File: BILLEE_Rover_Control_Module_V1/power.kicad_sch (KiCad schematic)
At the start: 86 parts, among them CN1 XT90PW-M.G.Y, CN2 XT60PW-M, CN3 XT60PW-M, CN4 XT60PW-M, CN5 XT60PW-M, SW1 33uH, U1 INA780BIDEKR, U2 MCP9808T-E/MS, U3 TPS1HA08BQPWPRQ1, U4 TPS1HA08BQPWPRQ1, U5 TPS1HA08BQPWPRQ1, U6 LT8612EUDE#TRPBF, U7 LT8612EUDE#TRPBF, U8 LT8612EUDE#TRPBF, U9 10uH

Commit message: continuing layout
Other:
- note added: "(+22.2v -> +12V) Network Switch and Aux Power"
- note removed: "+12V Network Switch and Aux Power"
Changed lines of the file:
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@@
 		)
 	)
-	(text "+12V Network Switch and Aux Power"
+	(text "(+22.2v -> +12V) Network Switch and Aux Power"
 		(exclude_from_sim no)
 		(at 96.012 171.958 0)
@@
 		)
 	)
-	(netclass_flag ""
-		(length 2.54)
-		(shape round)
-		(at 328.93 96.52 0)
-		(fields_autoplaced yes)
-		(effects
-			(font
-				(size 1.27 1.27)
-			)
-			(justify left bottom)
-		)
-		(property "Net Class" ""
-			(at 101.6 125.73 0)
-			(show_name no)
-			(do_not_autoplace no)
-			(effects
-				(font
-					(size 1.27 1.27)
-				)
-			)
-		)
-		(property "Component Class" "Jetsonregs"
-			(at 329.6285 93.98 0)
-			(show_name no)
-			(do_not_autoplace no)
-			(effects
-				(font
-					(size 1.27 1.27)
-					(italic yes)
-				)
-				(justify left)
-			)
-		)
-	)
 	(symbol
 		(lib_id "power:GND")
@@
 		(in_pos_files yes)
 		(dnp no)
-		(fields_autoplaced yes)
 		(property "Reference" "#PWR043"
 			(at 262.89 165.1 0)
@@
 		)
 		(property "Value" "GND"
-			(at 262.89 163.83 0)
+			(at 267.716 160.274 0)
 			(show_name no)
 			(do_not_autoplace no)

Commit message: Layout Cont.
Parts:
- removed TP2: TestPoint, TestPoint:TestPoint_THTPad_2.0x2.0mm_Drill1.0mm, symbol Connector:TestPoint
- added H1, H2, H3, H4: MountingHole_Pad, MountingHole:MountingHole_5.3mm_M5_Pad_Via, symbol Mechanical:MountingHole_Pad
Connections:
- net GND: now also CN4.3, CN4.4
- new net CHA_GND: H1.1, H2.1, H3.1, H4.1

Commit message: Layout! 🍋
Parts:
- H1, H2, H3, H4: footprint MountingHole:MountingHole_5.3mm_M5_Pad_Via -> MountingHole:MountingHole_4.3mm_M4_Pad_Via
- R22, R24, R26: value 180k -> 200k

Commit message: Layout!
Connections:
- net CHA_GND is gone; now on net GND: H1.1, H2.1, H3.1, H4.1
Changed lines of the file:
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@@
 	)
 	(junction
-		(at 52.07 184.15)
-		(diameter 0)
-		(color 0 0 0 0)
-	)
-	(junction
 		(at 59.69 133.35)
 		(diameter 0)
@@
 	)
 	(junction
+		(at 52.07 184.15)
+		(diameter 0)
+		(color 0 0 0 0)
+	)
+	(junction
 		(at 209.55 46.99)
 		(diameter 0)
@@
 	(wire
 		(pts
-			(xy 52.07 184.15) (xy 68.58 184.15)
-		)
-		(stroke
-			(width 0)
-			(type default)
-		)
-	)
-	(wire
-		(pts
 			(xy 134.62 187.96) (xy 171.45 187.96)
 		)
@@
 	(wire
 		(pts
+			(xy 52.07 184.15) (xy 68.58 184.15)
+		)
+		(stroke
+			(width 0)
+			(type default)
+		)
+	)
+	(wire
+		(pts
 			(xy 220.98 189.23) (xy 241.3 189.23)
 		)
@@
 	)
 	(symbol
-		(lib_id "power:GNDPWR")
-		(at 52.07 184.15 0)
-		(unit 1)
-		(body_style 1)
-		(exclude_from_sim no)
-		(in_bom yes)
-		(on_board yes)
-		(in_pos_files yes)
-		(dnp no)
-		(fields_autoplaced yes)
-		(property "Reference" "#PWR0209"
-			(at 52.07 189.23 0)
-			(hide yes)
-			(show_name no)
-			(do_not_autoplace no)
-			(effects
-				(font
-					(size 1.27 1.27)
-				)
-			)
-		)
-		(property "Value" "CHA_GND"
-			(at 51.943 187.96 0)
-			(show_name no)
-			(do_not_autoplace no)
-			(effects
-				(font
-					(size 1.27 1.27)
-				)
-			)
-		)
-		(property "Footprint" ""
-			(at 52.07 185.42 0)
-			(hide yes)
-			(show_name no)
-			(do_not_autoplace no)
-			(effects
-				(font
-					(size 1.27 1.27)
-				)
-			)
-		)
-		(property "Datasheet" ""
-			(at 52.07 185.42 0)
-			(hide yes)
-			(show_name no)
-			(do_not_autoplace no)
-			(effects
-				(font
-					(size 1.27 1.27)
-				)
-			)
-		)
-		(property "Description" "Power symbol creates a global label with name \"GNDPWR\" , global ground"
-			(at 52.07 184.15 0)
-			(hide yes)
-			(show_name no)
-			(do_not_autoplace no)
-			(effects
-				(font
-					(size 1.27 1.27)
-				)
-			)
-		)
-		(pin "1"
-		)
-		(instances
-			(project "BILLEE_Rover_Control_Module_V1"
-				(path "/e701dc98-f022-461d-84b5-6b2dd8d89d58/e37b5ac2-398e-41bf-8fb6-2ff87cb1df37"
-					(reference "#PWR0209")
-					(unit 1)
-				)
-			)
-		)
-	)
-	(symbol
 		(lib_id "power:GND")
 		(at 237.49 149.86 0)
@@
 					(unit 1)
 				)
+			)
+		)
+	)
+	(symbol
+		(lib_id "power:GND")
+		(at 52.07 184.15 0)
+		(unit 1)
+		(body_style 1)
+		(exclude_from_sim no)
+		(in_bom yes)
+		(on_board yes)
+		(in_pos_files yes)
+		(dnp no)
+		(fields_autoplaced yes)
+		(property "Reference" "#PWR0209"
+			(at 52.07 190.5 0)
+			(hide yes)
+			(show_name no)
+			(do_not_autoplace no)
+			(effects
+				(font
+					(size 1.27 1.27)
+				)
+			)
+		)
+		(property "Value" "GND"
+			(at 52.07 189.23 0)
+			(show_name no)
+			(do_not_autoplace no)
+			(effects
+				(font
+					(size 1.27 1.27)
+				)
+			)
+		)
+		(property "Footprint" ""
+			(at 52.07 184.15 0)
+			(hide yes)
+			(show_name no)
+			(do_not_autoplace no)
+			(effects
+				(font
+					(size 1.27 1.27)
+				)
+			)
+		)
+		(property "Datasheet" ""
+			(at 52.07 184.15 0)
+			(hide yes)
+			(show_name no)
+			(do_not_autoplace no)
+			(effects
+				(font
+					(size 1.27 1.27)
+				)
+			)
+		)
+		(property "Description" "Power symbol creates a global label with name \"GND\" , ground"
+			(at 52.07 184.15 0)
+			(hide yes)
+			(show_name no)
+			(do_not_autoplace no)
+			(effects
+				(font
+					(size 1.27 1.27)
+				)
+			)
+		)
+		(pin "1"
+		)
+		(instances
+			(project "BILLEE_Rover_Control_Module_V1"
+				(path "/e701dc98-f022-461d-84b5-6b2dd8d89d58/e37b5ac2-398e-41bf-8fb6-2ff87cb1df37"
+					(reference "#PWR0209")
+					(unit 1)
+				)

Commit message: More layout :tired_face:
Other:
- moved on the sheet: C12, C15, C18, C21, C24, C3, C6, C72, C9, CN4, CN5, D3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

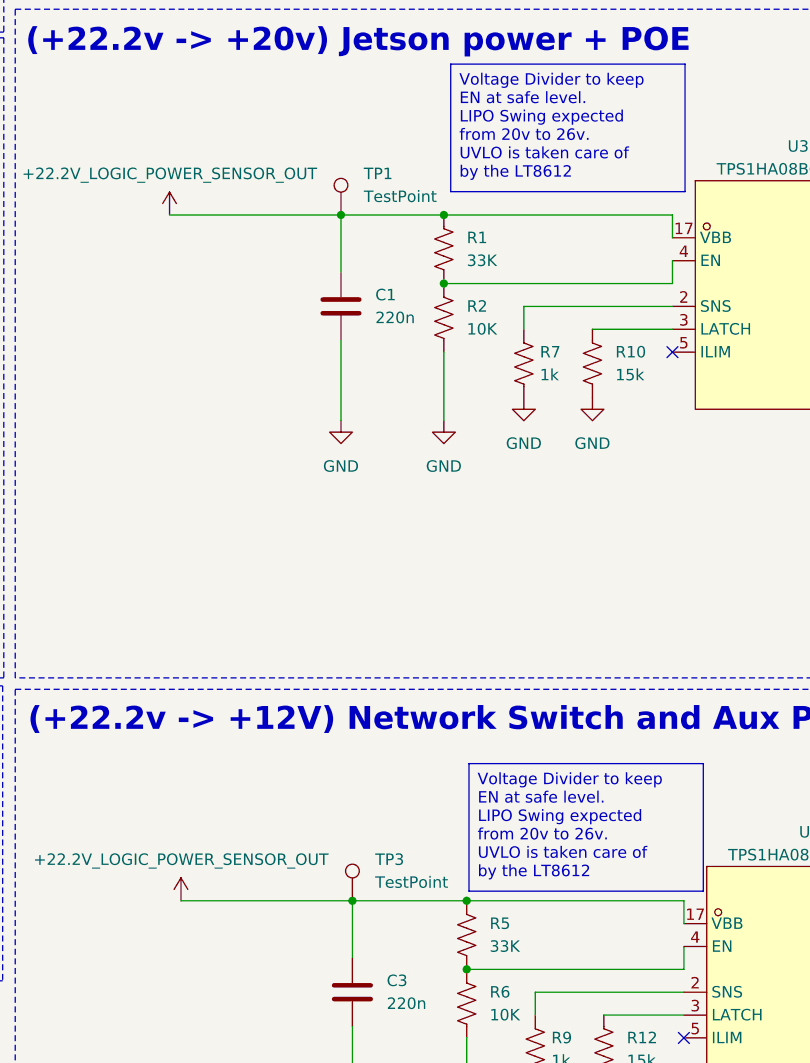
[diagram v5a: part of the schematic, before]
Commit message: Resatarted Layout for something a little bit cleaner.
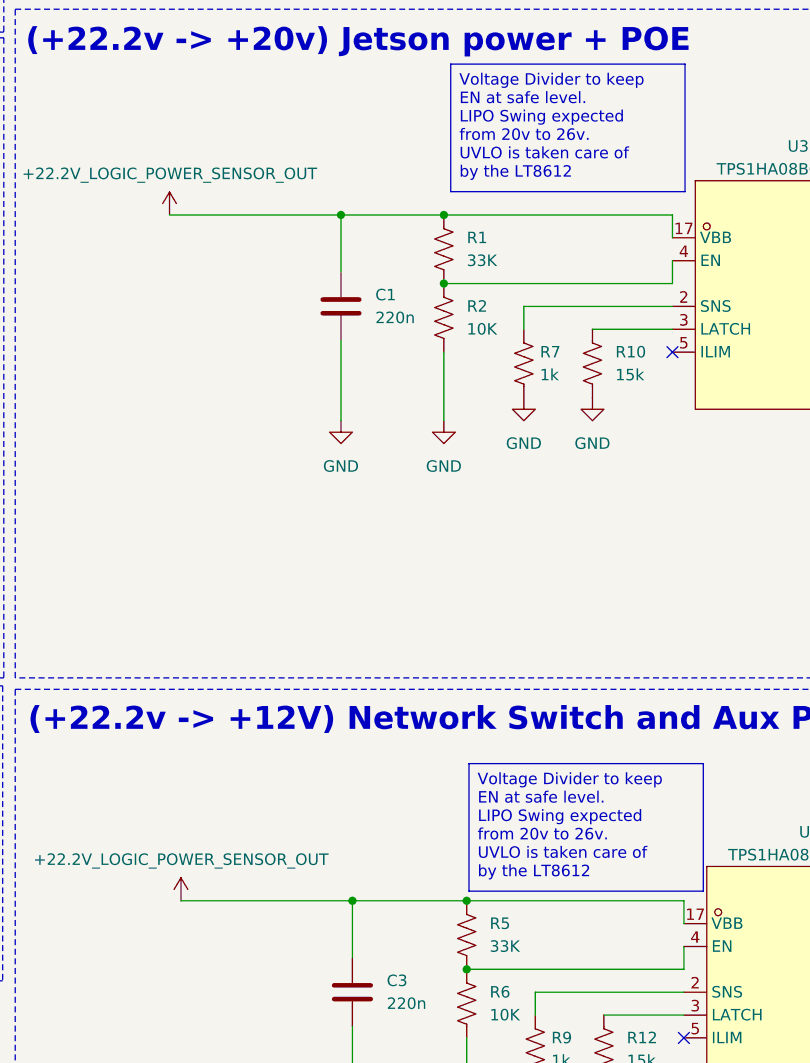
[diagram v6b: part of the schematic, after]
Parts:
- removed TP1, TP3: TestPoint, TestPoint:TestPoint_THTPad_2.0x2.0mm_Drill1.0mm, symbol Connector:TestPoint
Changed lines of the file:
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@@
 	)
 	(symbol
-		(lib_id "Connector:TestPoint")
-		(at 130.81 114.3 0)
-		(unit 1)
-		(body_style 1)
-		(exclude_from_sim no)
-		(in_bom yes)
-		(on_board yes)
-		(in_pos_files yes)
-		(dnp no)
-		(fields_autoplaced yes)
-		(property "Reference" "TP1"
-			(at 133.35 109.7279 0)
-			(show_name no)
-			(do_not_autoplace no)
-			(effects
-				(font
-					(size 1.27 1.27)
-				)
-				(justify left)
-			)
-		)
-		(property "Value" "TestPoint"
-			(at 133.35 112.2679 0)
-			(show_name no)
-			(do_not_autoplace no)
-			(effects
-				(font
-					(size 1.27 1.27)
-				)
-				(justify left)
-			)
-		)
-		(property "Footprint" "TestPoint:TestPoint_THTPad_2.0x2.0mm_Drill1.0mm"
-			(at 135.89 114.3 0)
-			(hide yes)
-			(show_name no)
-			(do_not_autoplace no)
-			(effects
-				(font
-					(size 1.27 1.27)
-				)
-			)
-		)
-		(property "Datasheet" ""
-			(at 135.89 114.3 0)
-			(hide yes)
-			(show_name no)
-			(do_not_autoplace no)
-			(effects
-				(font
-					(size 1.27 1.27)
-				)
-			)
-		)
-		(property "Description" "test point"
-			(at 130.81 114.3 0)
-			(hide yes)
-			(show_name no)
-			(do_not_autoplace no)
-			(effects
-				(font
-					(size 1.27 1.27)
-				)
-			)
-		)
-		(pin "1"
-		)
-		(instances
-			(project "BILLEE_Rover_Control_Module_V1"
-				(path "/e701dc98-f022-461d-84b5-6b2dd8d89d58/e37b5ac2-398e-41bf-8fb6-2ff87cb1df37"
-					(reference "TP1")
-					(unit 1)
-				)
-			)
-		)
-	)
-	(symbol
 		(lib_id "power:+3.3V")
 		(at 326.39 41.91 0)
@@
 					(unit 1)
 				)
-			)
-		)
-	)
-	(symbol
-		(lib_id "Connector:TestPoint")
-		(at 132.08 190.5 0)
-		(unit 1)
-		(body_style 1)
-		(exclude_from_sim no)
-		(in_bom yes)
-		(on_board yes)
-		(in_pos_files yes)
-		(dnp no)
-		(fields_autoplaced yes)
-		(property "Reference" "TP3"
-			(at 134.62 185.9279 0)
-			(show_name no)
-			(do_not_autoplace no)
-			(effects
-				(font
-					(size 1.27 1.27)
-				)
-				(justify left)
-			)
-		)
-		(property "Value" "TestPoint"
-			(at 134.62 188.4679 0)
-			(show_name no)
-			(do_not_autoplace no)
-			(effects
-				(font
-					(size 1.27 1.27)
-				)
-				(justify left)
-			)
-		)
-		(property "Footprint" "TestPoint:TestPoint_THTPad_2.0x2.0mm_Drill1.0mm"
-			(at 137.16 190.5 0)
-			(hide yes)
-			(show_name no)
-			(do_not_autoplace no)
-			(effects
-				(font
-					(size 1.27 1.27)
-				)
-			)
-		)
-		(property "Datasheet" ""
-			(at 137.16 190.5 0)
-			(hide yes)
-			(show_name no)
-			(do_not_autoplace no)
-			(effects
-				(font
-					(size 1.27 1.27)
-				)
-			)
-		)
-		(property "Description" "test point"
-			(at 132.08 190.5 0)
-			(hide yes)
-			(show_name no)
-			(do_not_autoplace no)
-			(effects
-				(font
-					(size 1.27 1.27)
-				)
-			)
-		)
-		(pin "1"
-		)
-		(instances
-			(project "BILLEE_Rover_Control_Module_V1"
-				(path "/e701dc98-f022-461d-84b5-6b2dd8d89d58/e37b5ac2-398e-41bf-8fb6-2ff87cb1df37"
-					(reference "TP3")
-					(unit 1)
-				)

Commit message: Routing complete I think
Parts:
- C19, C22: value 47u -> 10u
- C21, C24: Voltage 50V -> 25V
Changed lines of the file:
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@@
 			)
 		)
-		(property "Value" "47u"
+		(property "Value" "10u"
 			(at 318.77 121.666 0)
 			(show_name no)
@@
 			)
 		)
-		(property "Voltage" "50V"
+		(property "Voltage" "25V"
 			(at 328.93 204.47 0)
 			(show_name no)
@@
 			)
 		)
-		(property "Voltage" "50V"
+		(property "Voltage" "25V"
 			(at 317.5 204.47 0)
 			(show_name no)
@@
 			)
 		)
-		(property "Value" "47u"
+		(property "Value" "10u"
 			(at 330.2 121.666 0)
 			(show_name no)

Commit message: Done I think
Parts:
- C20, C21, C23, C24: value 47u -> 10u
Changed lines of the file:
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@@
 			)
 		)
-		(property "Value" "47u"
+		(property "Value" "10u"
 			(at 331.47 197.866 0)
 			(show_name no)
@@
 			)
 		)
-		(property "Value" "47u"
+		(property "Value" "10u"
 			(at 332.74 45.466 0)
 			(show_name no)
@@
 			)
 		)
-		(property "Value" "47u"
+		(property "Value" "10u"
 			(at 321.31 45.466 0)
 			(show_name no)
@@
 			)
 		)
-		(property "Value" "47u"
+		(property "Value" "10u"
 			(at 320.04 197.866 0)
 			(show_name no)
